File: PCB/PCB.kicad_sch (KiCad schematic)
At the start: 52 parts, among them J1 Conn_01x02_Socket, J2 Conn_01x02_Pin, J3 Conn_01x02_Pin, J4 Conn_01x02_Socket, J5 Programming Pin, J6 Programming Pin, J7 Programming Pin, J8 Programming Pin, U1 STM32L476RGTx, U2 FGPMMOPA6H, U4 TPS63001DRCR, U5 LM2735XMF/NOPB, U8 LM386, U9 MAX7375AXR805

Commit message: Add files via upload
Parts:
- removed FB2, FB3: FerriteBead, Ferrite_THT:LairdTech_28C0236-0JW-10, symbol Device:FerriteBead
- C1, C11, C2, C4: footprint Capacitor_SMD:C_0805_2012Metric -> Capacitor_SMD:C_0805_2012Metric_Pad1.18x1.45mm_HandSolder
- C10, C12, C13, C14, C15, C16, C17, C19: footprint (none) -> Capacitor_SMD:C_0805_2012Metric_Pad1.18x1.45mm_HandSolder
- C3, C5: footprint Resistor_SMD:R_0805_2012Metric -> Capacitor_SMD:C_0805_2012Metric_Pad1.18x1.45mm_HandSolder
- FB1, FB4: footprint (none) -> Ferrite_THT:LairdTech_28C0236-0JW-10
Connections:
- net +3.3 VD is gone; now on net GND: C10.1, C10.2, C13.1, C13.2, C14.1, C14.2, C15.1, C15.2, FB1.1, FB4.1
- net Earth: now also U1.12 (VSSA)
- net GND: now reaches C19.1, C2.1, U1.1 (VBAT), U1.19 (VDD), U1.32 (VDD), U1.48 (VDDUSB), U1.64 (VDD), U2.P$1 (VCC), U2.P$4 (VBACKUP), U3.1 (VDD), U3.2 (NRST), U4.1 (VOUT), U4.10 (FB), U9.1 (V+)
- net VDDA Connection: now reaches U1.13 (VDDA)
- net VDDA Connection: now also C16.1, C17.1, FB1.2
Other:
- moved on the sheet: J7, J8

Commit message: Add files via upload
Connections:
- net GND is gone; now on net Earth: C10.1, C10.2, C13.1, C13.2, C14.1, C14.2, C15.1, C15.2, C19.1, C2.1, FB1.1, FB4.1, U1.1 (VBAT), U1.19 (VDD), U1.32 (VDD), U1.48 (VDDUSB), U1.64 (VDD), U2.P$1 (VCC), U2.P$4 (VBACKUP), U3.1 (VDD), U3.2 (NRST), U4.1 (VOUT), U4.10 (FB), U9.1 (V+)
- net Earth: no longer U1.12 (VSSA)
- net VDDA GND Connection: now reaches C16.2, C17.2, FB4.2
- net VDDA GND Connection: now also U1.12 (VSSA)
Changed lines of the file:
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@@
 	)
 	(junction
-		(at 237.49 153.67)
-		(diameter 0)
-		(color 0 0 0 0)
-	)
-	(junction
 		(at 223.52 17.78)
 		(diameter 0)
@@
 	)
 	(junction
-		(at 116.84 173.99)
-		(diameter 0)
-		(color 0 0 0 0)
-	)
-	(junction
 		(at 69.85 160.02)
 		(diameter 0)
@@
 	)
 	(junction
-		(at 116.84 168.91)
-		(diameter 0)
-		(color 0 0 0 0)
-	)
-	(junction
 		(at 209.55 17.78)
 		(diameter 0)
@@
 	(wire
 		(pts
-			(xy 171.45 168.91) (xy 171.45 173.99)
-		)
-		(stroke
-			(width 0)
-			(type default)
-		)
-	)
-	(wire
-		(pts
 			(xy 220.98 81.28) (xy 220.98 92.71)
 		)
@@
 	(wire
 		(pts
-			(xy 233.68 153.67) (xy 237.49 153.67)
-		)
-		(stroke
-			(width 0)
-			(type default)
-		)
-	)
-	(wire
-		(pts
 			(xy 220.98 104.14) (xy 226.06 104.14)
 		)
@@
 	(wire
 		(pts
-			(xy 116.84 173.99) (xy 116.84 181.61)
-		)
-		(stroke
-			(width 0)
-			(type default)
-		)
-	)
-	(wire
-		(pts
 			(xy 227.33 143.51) (xy 233.68 143.51)
 		)
@@
 	(wire
 		(pts
-			(xy 116.84 162.56) (xy 116.84 168.91)
-		)
-		(stroke
-			(width 0)
-			(type default)
-		)
-	)
-	(wire
-		(pts
 			(xy 62.23 190.5) (xy 34.29 190.5)
 		)
@@
 	(wire
 		(pts
-			(xy 237.49 153.67) (xy 241.3 153.67)
+			(xy 233.68 153.67) (xy 241.3 153.67)
 		)
 		(stroke
@@
 	(wire
 		(pts
-			(xy 116.84 168.91) (xy 116.84 173.99)
+			(xy 116.84 162.56) (xy 116.84 181.61)
 		)
 		(stroke
@@
 	(wire
 		(pts
-			(xy 168.91 168.91) (xy 116.84 168.91)
-		)
-		(stroke
-			(width 0)
-			(type default)
-		)
-	)
-	(wire
-		(pts
 			(xy 250.19 90.17) (xy 250.19 104.14)
 		)
@@
 	(wire
 		(pts
-			(xy 116.84 173.99) (xy 171.45 173.99)
-		)
-		(stroke
-			(width 0)
-			(type default)
-		)
-	)
-	(wire
-		(pts
 			(xy 62.23 133.35) (xy 62.23 190.5)
 		)
@@
 		)
 	)
+	(global_label "VDDA GND Connection"
+		(shape output)
+		(at 171.45 168.91 270)
+		(fields_autoplaced yes)
+		(effects
+			(font
+				(size 1.27 1.27)
+			)
+			(justify right)
+		)
+		(property "Intersheetrefs" "${INTERSHEET_REFS}"
+			(at 171.45 192.9408 90)
+			(effects
+				(font
+					(size 1.27 1.27)
+				)
+				(justify right)
+				(hide yes)
+			)
+		)
+	)
 	(global_label "PAD"
 		(shape bidirectional)
@@
 		)
 	)
+	(global_label "Ground"
+		(shape output)
+		(at 237.49 153.67 270)
+		(fields_autoplaced yes)
+		(effects
+			(font
+				(size 1.27 1.27)
+			)
+			(justify right)
+		)
+		(property "Intersheetrefs" "${INTERSHEET_REFS}"
+			(at 237.49 163.3074 90)
+			(effects
+				(font
+					(size 1.27 1.27)
+				)
+				(justify right)
+				(hide yes)
+			)
+		)
+	)
+	(global_label "VDDA GND Connection"
+		(shape input)
+		(at 261.62 153.67 0)
+		(fields_autoplaced yes)
+		(effects
+			(font
+				(size 1.27 1.27)
+			)
+			(justify left)
+		)
+		(property "Intersheetrefs" "${INTERSHEET_REFS}"
+			(at 285.6508 153.67 0)
+			(effects
+				(font
+					(size 1.27 1.27)
+				)
+				(justify left)
+				(hide yes)
+			)
+		)
+	)
 	(global_label "VDDA Connection"
 		(shape input)
@@
 		)
 	)
+	(global_label "Ground"
+		(shape input)
+		(at 116.84 171.45 0)
+		(fields_autoplaced yes)
+		(effects
+			(font
+				(size 1.27 1.27)
+			)
+			(justify left)
+		)
+		(property "Intersheetrefs" "${INTERSHEET_REFS}"
+			(at 126.4774 171.45 0)
+			(effects
+				(font
+					(size 1.27 1.27)
+				)
+				(justify left)
+				(hide yes)
+			)
+		)
+	)
 	(global_label "VDDA Connection"
 		(shape output)
@@
 		)
 	)
+	(global_label "Ground"
+		(shape output)
+		(at 168.91 168.91 270)
+		(fields_autoplaced yes)
+		(effects
+			(font
+				(size 1.27 1.27)
+			)
+			(justify right)
+		)
+		(property "Intersheetrefs" "${INTERSHEET_REFS}"
+			(at 168.91 178.5474 90)
+			(effects
+				(font
+					(size 1.27 1.27)
+				)
+				(justify right)
+				(hide yes)
+			)
+		)
+	)
 	(symbol
 		(lib_id "Device:D")
@@
 					(unit 1)
 				)
-			)
-		)
-	)
-	(symbol
-		(lib_id "power:GND")
-		(at 237.49 153.67 0)
-		(unit 1)
-		(exclude_from_sim no)
-		(in_bom yes)
-		(on_board yes)
-		(dnp no)
-		(fields_autoplaced yes)
-		(property "Reference" "#PWR02"
-			(at 237.49 160.02 0)
-			(effects
-				(font
-					(size 1.27 1.27)
-				)
-				(hide yes)
-			)
-		)
-		(property "Value" "GND"
-			(at 237.49 158.75 0)
-			(effects
-				(font
-					(size 1.27 1.27)
-				)
-			)
-		)
-		(property "Footprint" ""
-			(at 237.49 153.67 0)
-			(effects
-				(font
-					(size 1.27 1.27)
-				)
-				(hide yes)
-			)
-		)
-		(property "Datasheet" ""
-			(at 237.49 153.67 0)
-			(effects
-				(font
-					(size 1.27 1.27)
-				)
-				(hide yes)
-			)
-		)
-		(property "Description" "Power symbol creates a global label with name \"GND\" , ground"
-			(at 237.49 153.67 0)
-			(effects
-				(font
-					(size 1.27 1.27)
-				)
-				(hide yes)
-			)
-		)
-		(pin "1"
-		)
-		(instances
-			(project "PCB"
-				(path "/eb9a8801-b205-4599-90e8-b0089b4de1f9"
-					(reference "#PWR02")
-					(unit 1)
-				)

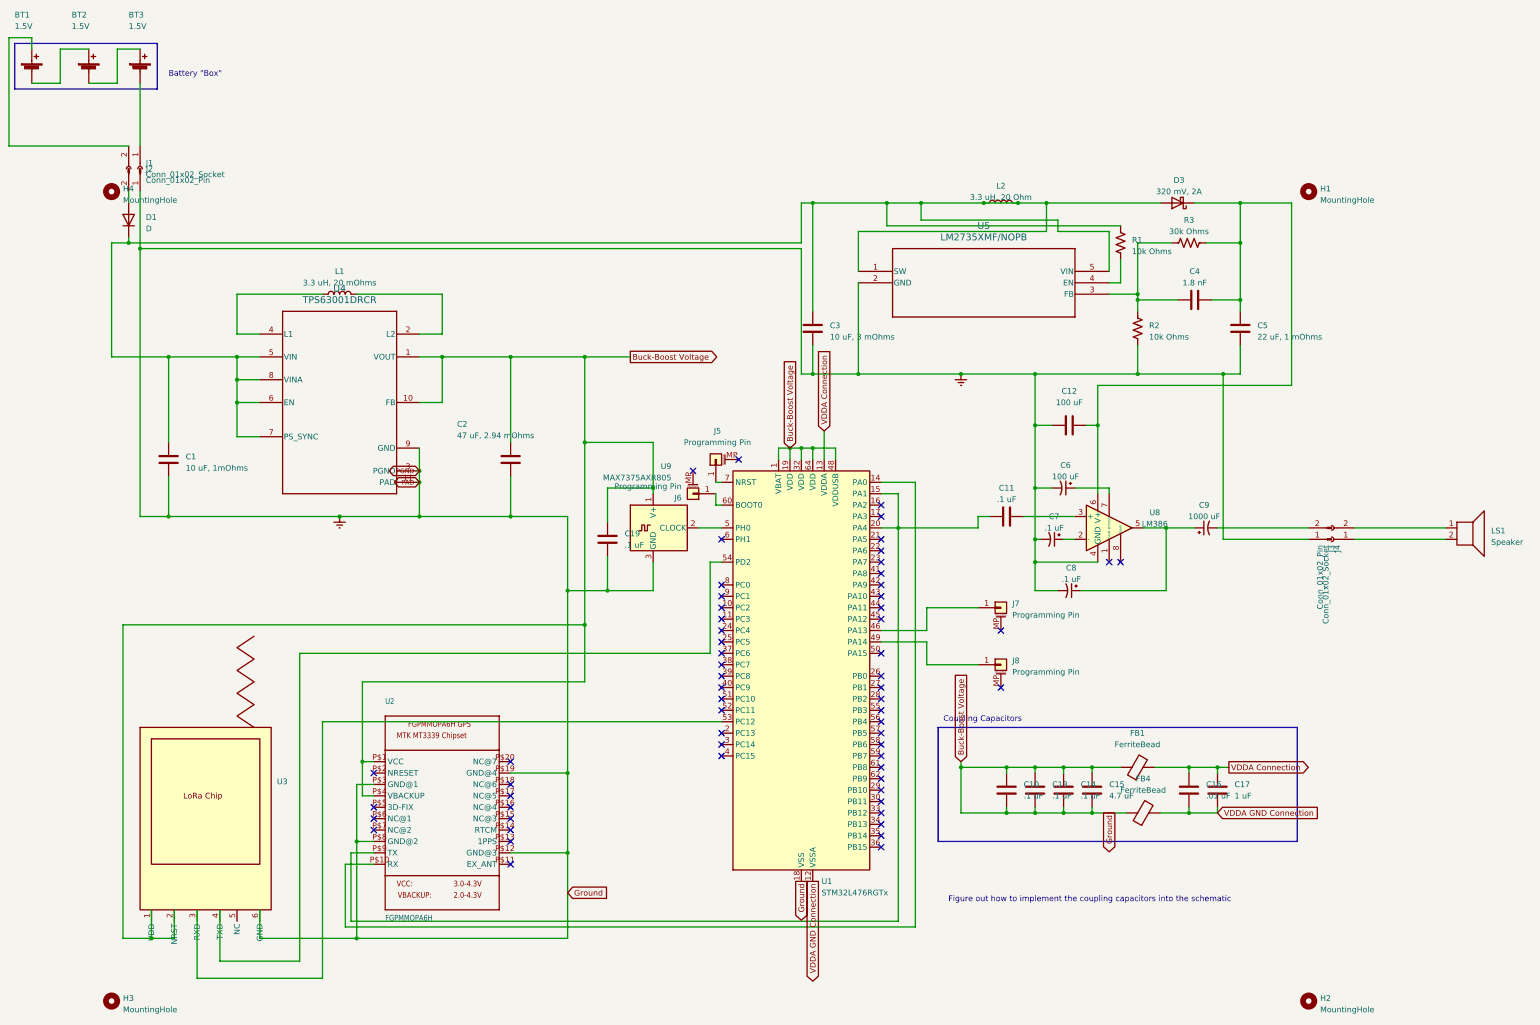
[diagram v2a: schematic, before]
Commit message: Add files via upload
Need to decide how big the ground plane is, where to place the GPS, and connect the LoRa and GPS traces.
Also need to add silkscreen layer and make sure checks in PCB verification checklist are completed.
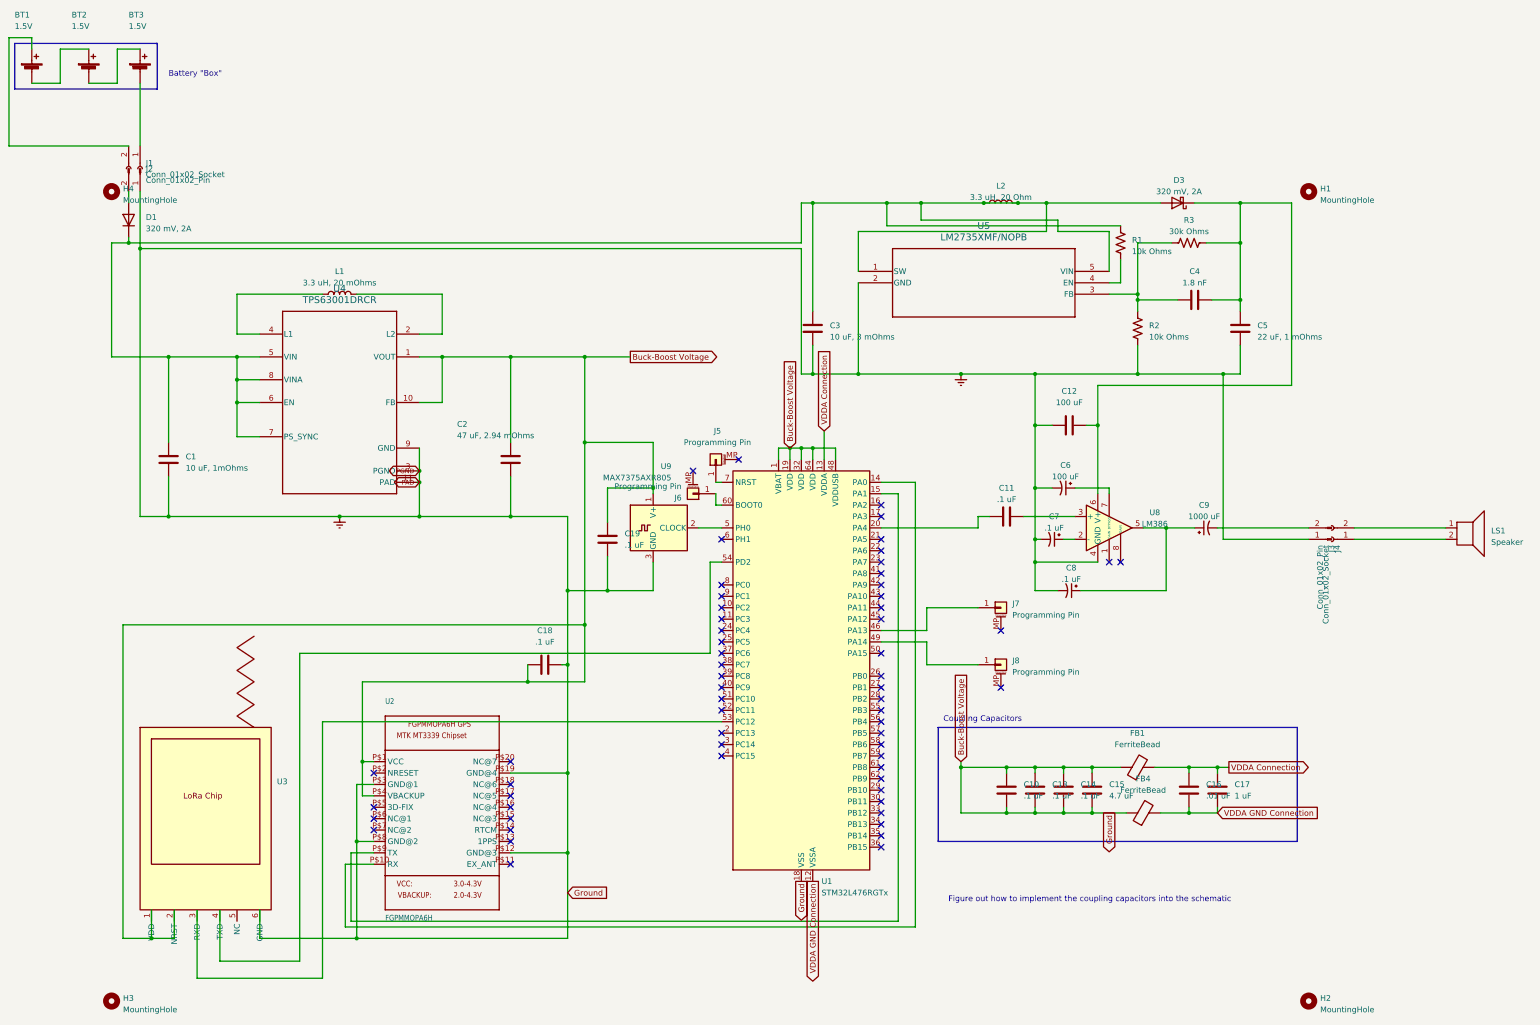
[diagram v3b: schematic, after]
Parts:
- added C18: .1 uF, Capacitor_SMD:C_0805_2012Metric_Pad1.18x1.45mm_HandSolder, symbol Device:C
- D1: value D -> 320 mV, 2A
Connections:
- net Earth: now also C18.1, C18.2
- net at C11.1, U1.20 (PA4): no longer U1.15 (PA1), U2.P$9 (TX)
- new net: U1.15 (PA1), U2.P$9 (TX)
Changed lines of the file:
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@@
 	)
 	(junction
+		(at 116.84 120.65)
+		(diameter 0)
+		(color 0 0 0 0)
+	)
+	(junction
 		(at 255.27 143.51)
 		(diameter 0)
@@
 	)
 	(junction
+		(at 107.95 124.46)
+		(diameter 0)
+		(color 0 0 0 0)
+	)
+	(junction
 		(at 266.7 17.78)
 		(diameter 0)
@@
 	)
 	(junction
-		(at 190.5 90.17)
-		(diameter 0)
-		(color 0 0 0 0)
-	)
-	(junction
 		(at 181.61 55.88)
 		(diameter 0)
@@
 	(wire
 		(pts
+			(xy 116.84 120.65) (xy 116.84 144.78)
+		)
+		(stroke
+			(width 0)
+			(type default)
+		)
+	)
+	(wire
+		(pts
 			(xy 57.15 118.11) (xy 57.15 186.69)
 		)
@@
 	(wire
 		(pts
-			(xy 190.5 90.17) (xy 208.28 90.17)
-		)
-		(stroke
-			(width 0)
-			(type default)
-		)
-	)
-	(wire
-		(pts
 			(xy 234.95 58.42) (xy 234.95 67.31)
 		)
@@
 	(wire
 		(pts
-			(xy 190.5 82.55) (xy 190.5 90.17)
+			(xy 190.5 82.55) (xy 190.5 177.8)
 		)
 		(stroke
@@
 	(wire
 		(pts
-			(xy 186.69 90.17) (xy 190.5 90.17)
+			(xy 186.69 90.17) (xy 208.28 90.17)
 		)
 		(stroke
@@
 	(wire
 		(pts
+			(xy 115.57 120.65) (xy 116.84 120.65)
+		)
+		(stroke
+			(width 0)
+			(type default)
+		)
+	)
+	(wire
+		(pts
 			(xy 243.84 49.53) (xy 243.84 55.88)
 		)
@@
 	(wire
 		(pts
+			(xy 107.95 120.65) (xy 107.95 124.46)
+		)
+		(stroke
+			(width 0)
+			(type default)
+		)
+	)
+	(wire
+		(pts
 			(xy 125.73 81.28) (xy 125.73 88.9)
 		)
@@
 	(wire
 		(pts
-			(xy 116.84 104.14) (xy 116.84 144.78)
+			(xy 116.84 104.14) (xy 116.84 120.65)
 		)
 		(stroke
@@
 	(wire
 		(pts
-			(xy 190.5 90.17) (xy 190.5 177.8)
+			(xy 243.84 26.67) (xy 251.46 26.67)
 		)
 		(stroke
@@
 	(wire
 		(pts
-			(xy 243.84 26.67) (xy 251.46 26.67)
+			(xy 116.84 87.63) (xy 116.84 104.14)
 		)
 		(stroke
@@
 	(wire
 		(pts
-			(xy 116.84 87.63) (xy 116.84 104.14)
+			(xy 15.24 26.67) (xy 19.05 26.67)
 		)
 		(stroke
@@
 	(wire
 		(pts
-			(xy 15.24 26.67) (xy 19.05 26.67)
+			(xy 120.65 124.46) (xy 120.65 111.76)
 		)
 		(stroke
@@
 	(wire
 		(pts
-			(xy 120.65 124.46) (xy 120.65 111.76)
+			(xy 107.95 124.46) (xy 120.65 124.46)
 		)
 		(stroke
@@
 	(wire
 		(pts
-			(xy 71.12 124.46) (xy 120.65 124.46)
+			(xy 71.12 124.46) (xy 107.95 124.46)
 		)
 		(stroke
@@
 			)
 		)
-		(property "Value" "D"
+		(property "Value" "320 mV, 2A"
 			(at 22.86 23.495 90)
 			(effects
@@
 					(unit 1)
 				)
+			)
+		)
+	)
+	(symbol
+		(lib_id "Device:C")
+		(at 111.76 120.65 90)
+		(unit 1)
+		(exclude_from_sim no)
+		(in_bom yes)
+		(on_board yes)
+		(dnp no)
+		(fields_autoplaced yes)
+		(property "Reference" "C18"
+			(at 111.76 113.03 90)
+			(effects
+				(font
+					(size 1.27 1.27)
+				)
+			)
+		)
+		(property "Value" ".1 uF"
+			(at 111.76 115.57 90)
+			(effects
+				(font
+					(size 1.27 1.27)
+				)
+			)
+		)
+		(property "Footprint" "Capacitor_SMD:C_0805_2012Metric_Pad1.18x1.45mm_HandSolder"
+			(at 115.57 119.6848 0)
+			(effects
+				(font
+					(size 1.27 1.27)
+				)
+				(hide yes)
+			)
+		)
+		(property "Datasheet" "~"
+			(at 111.76 120.65 0)
+			(effects
+				(font
+					(size 1.27 1.27)
+				)
+				(hide yes)
+			)
+		)
+		(property "Description" "Unpolarized capacitor"
+			(at 111.76 120.65 0)
+			(effects
+				(font
+					(size 1.27 1.27)
+				)
+				(hide yes)
+			)
+		)
+		(pin "2"
+		)
+		(pin "1"
+		)
+		(instances
+			(project ""
+				(path "/eb9a8801-b205-4599-90e8-b0089b4de1f9"
+					(reference "C18")
+					(unit 1)
+				)
